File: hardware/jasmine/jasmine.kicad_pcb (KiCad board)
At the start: 2 copper layers, 70.7 x 53.3 mm, 28 parts, among them J1 NEIGHBOR1, J2 NEIGHBOR2, J3 USB-MICRO-B-SHIELDED, J4 LIPO_BATT_CONN, J7 BONUS_ROW, P1 TEST_POINT, P2 TEST_POINT, P3 TEST_POINT, P4 TEST_POINT, P5 3.7_VDC, U1 MCP73831T

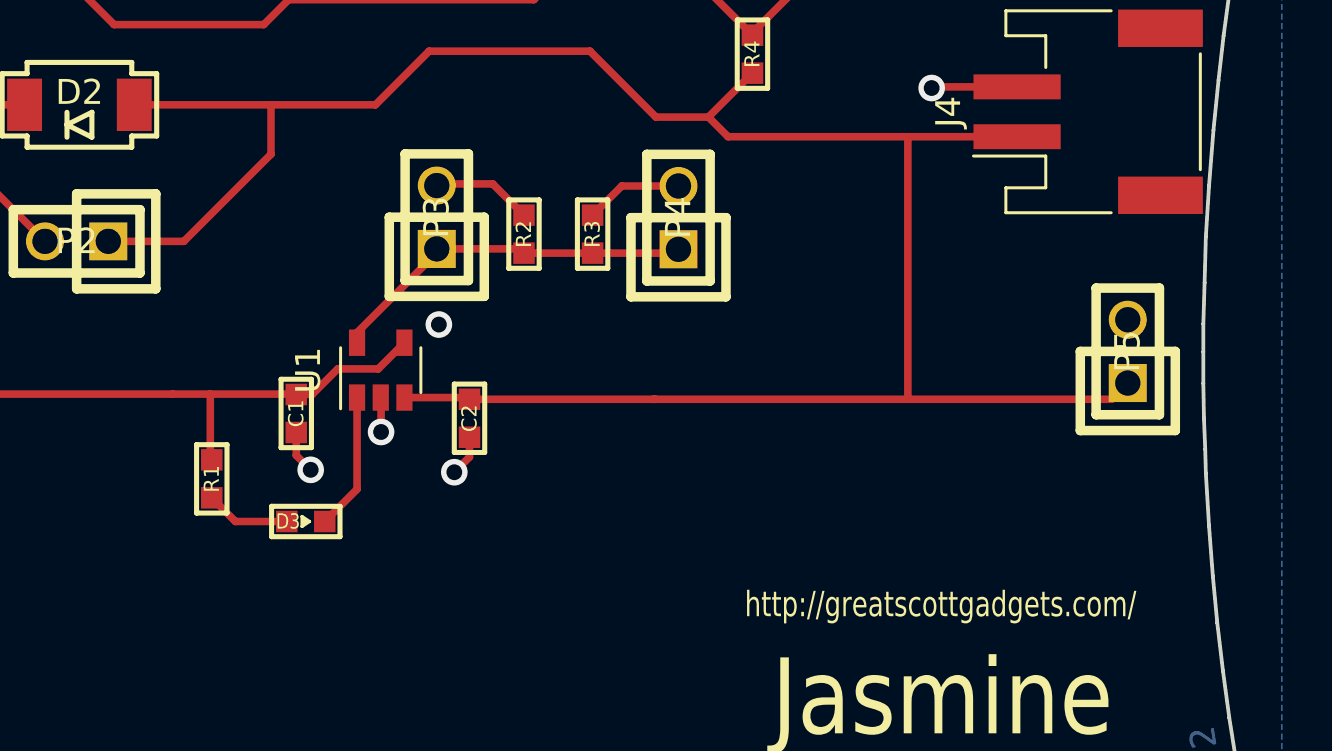
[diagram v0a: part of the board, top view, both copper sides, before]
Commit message: Cleaning up GF and jasmine to fix local repo
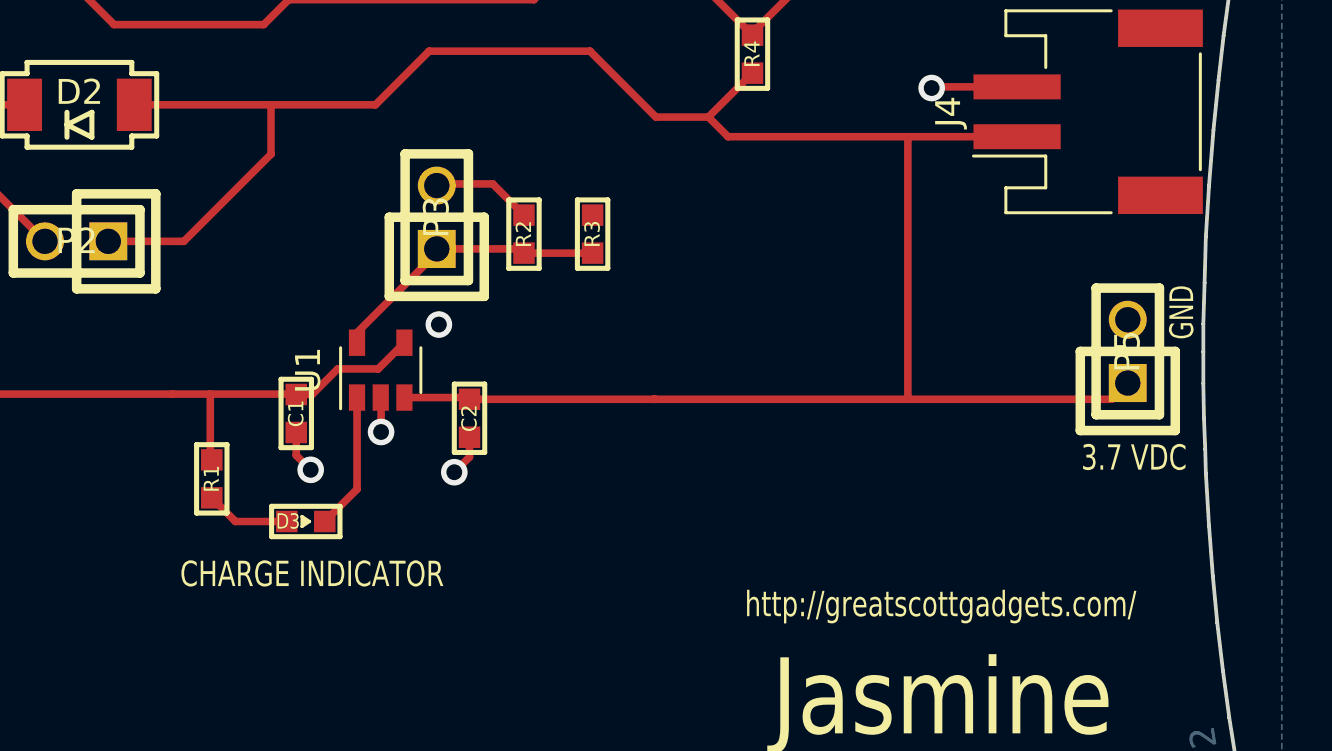
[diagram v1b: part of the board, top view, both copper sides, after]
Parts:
- removed P4: TEST_POINT, gsg-modules:HEADER-1x2
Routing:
- net GND: track 19.6 -> 15.7 mm
- net Net-(P3-Pad1): track 14.9 -> 11.4 mm
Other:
- board text added: "3.7 VDC"
- board text added: "CHARGE INDICATOR"
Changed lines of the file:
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@@
-(kicad_pcb (version 4) (host pcbnew 4.0.5+dfsg1-4)
+(kicad_pcb (version 4) (host pcbnew 4.0.6+dfsg1-1)
   (general
-    (links 94)
-    (no_connects 4)
+    (links 92)
+    (no_connects 5)
     (area 97.051224 67 279.525801 123.000001)
     (thickness 1.6)
-    (drawings 120)
-    (tracks 127)
+    (drawings 123)
+    (tracks 123)
     (zones 0)
-    (modules 28)
+    (modules 27)
     (nets 107)
   )
@@
       (net 1 GND))
   )
-  (module gsg-modules:HEADER-1x2 (layer F.Cu)
-    (at 156.79928 89.74328 90)
-    (tags CONN)
-    (fp_text reference P4 (at 0 0 90) (layer F.SilkS)
-      (effects (font (size 1.016 1.016) (thickness 0.2032)))
-    )
-    (fp_text value TEST_POINT (at 0 0 90) (layer F.SilkS) hide
-      (effects (font (size 1.016 1.016) (thickness 0.2032)))
-    )
-    (fp_line (start -2.54 -1.27) (end 2.54 -1.27) (layer F.SilkS) (width 0.381))
-    (fp_line (start 2.54 -1.27) (end 2.54 1.27) (layer F.SilkS) (width 0.381))
-    (fp_line (start 2.54 1.27) (end -2.54 1.27) (layer F.SilkS) (width 0.381))
-    (fp_line (start 0 1.905) (end 0 -1.905) (layer F.SilkS) (width 0.381))
-    (fp_line (start 0 -1.905) (end -3.175 -1.905) (layer F.SilkS) (width 0.381))
-    (fp_line (start -3.175 -1.905) (end -3.175 1.905) (layer F.SilkS) (width 0.381))
-    (fp_line (start -2.54 -1.27) (end -2.54 1.27) (layer F.SilkS) (width 0.381))
-    (fp_line (start -3.175 1.905) (end 0 1.905) (layer F.SilkS) (width 0.381))
-    (pad 1 thru_hole rect (at -1.27 0 90) (size 1.524 1.524) (drill 1.016) (layers *.Cu *.Mask F.SilkS)
-      (net 102 "Net-(P3-Pad1)"))
-    (pad 2 thru_hole circle (at 1.27 0 90) (size 1.524 1.524) (drill 1.016) (layers *.Cu *.Mask F.SilkS)
-      (net 1 GND))
-  )
   (module gsg-modules:0603 (layer F.Cu)
     (at 138.08 100.22 270)
@@
       (rotate (xyz 0 0 0))
     )
+  )
+  (gr_text "3.7 VDC" (at 175.07 99.38) (layer F.SilkS)
+    (effects (font (size 1.016 0.762) (thickness 0.1905)))
+  )
+  (gr_text GND (at 177 93.54 90) (layer F.SilkS)
+    (effects (font (size 0.9525 0.6985) (thickness 0.174625)))
+  )
+  (gr_text "CHARGE INDICATOR" (at 142.1 104.05) (layer F.SilkS)
+    (effects (font (size 1.016 0.762) (thickness 0.1905)))
   )
   (gr_line (start 109.6772 98.933) (end 109.728 99.9998) (angle 90) (layer Edge.Cuts) (width 0.15))
@@
   (segment (start 144.87 96.9734) (end 144.87 98.34) (width 0.3048) (layer F.Cu) (net 1))
   (via (at 144.87 98.34) (size 1.0668) (drill 0.635) (layers F.Cu B.Cu) (net 1))
-  (segment (start 153.35504 89.64168) (end 154.52344 88.47328) (width 0.3048) (layer F.Cu) (net 1))
-  (segment (start 154.52344 88.47328) (end 156.79928 88.47328) (width 0.3048) (layer F.Cu) (net 1))
   (segment (start 150.60168 89.64168) (end 149.35 88.39) (width 0.3048) (layer F.Cu) (net 1))
   (segment (start 149.35 88.39) (end 147.1696 88.39) (width 0.3048) (layer F.Cu) (net 1))
@@
   (segment (start 142 78) (end 141 77) (width 0.3048) (layer F.Cu) (net 58))
   (segment (start 146.3133 78) (end 142 78) (width 0.3048) (layer F.Cu) (net 58))
-  (segment (start 153.35504 91.16568) (end 156.64688 91.16568) (width 0.3048) (layer F.Cu) (net 102))
-  (segment (start 156.64688 91.16568) (end 156.79928 91.01328) (width 0.3048) (layer F.Cu) (net 102))
   (segment (start 150.60168 91.16568) (end 153.35504 91.16568) (width 0.3048) (layer F.Cu) (net 102))
   (segment (start 147.1041 90.9955) (end 150.4315 90.9955) (width 0.3048) (layer F.Cu) (net 102))
